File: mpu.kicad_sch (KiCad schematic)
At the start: 25 parts, among them SW401 SW_DIP_x03, U401 STM32MP135FAE7, Y401 32.768 kHz, Y402 24 MHz

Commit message: Update BOM, and fix MPU pinout
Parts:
- removed R404: 10 kΩ, Resistor_SMD:R_0201_0603Metric, symbol Device:R
- added D401, D402: 150060RS75000, LED_SMD:LED_0603_1608Metric, symbol Device:LED
- added R403: 10 kΩ, perfect_footprints:R_0201_0603Metric, symbol Device:R
- added R405, R406: 1 kΩ, perfect_footprints:R_0201_0603Metric, symbol Device:R
- added TP406, TP407: TestPoint, TestPoint:TestPoint_Pad_D1.0mm, symbol Connector:TestPoint
- C401, C402, C403, C404, C405, C406: footprint Capacitor_SMD:C_0201_0603Metric -> perfect_footprints:C_0201_0603Metric
- R401: footprint Resistor_SMD:R_0201_0603Metric -> perfect_footprints:R_0201_0603Metric
- R402: renamed from R403; footprint Resistor_SMD:R_0201_0603Metric -> perfect_footprints:R_0201_0603Metric
- R404: renamed from R402; footprint Resistor_SMD:R_0201_0603Metric -> perfect_footprints:R_0201_0603Metric; now fitted
- R407: renamed from R405; footprint Resistor_SMD:R_0201_0603Metric -> perfect_footprints:R_0201_0603Metric
- R408: renamed from R406; footprint Resistor_SMD:R_0201_0603Metric -> perfect_footprints:R_0201_0603Metric
- R409: renamed from R407; footprint Resistor_SMD:R_0201_0603Metric -> perfect_footprints:R_0201_0603Metric
- renumbered TP406 to TP408, TP407 to TP409, TP408 to TP410
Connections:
- net DEBUG.RX: now also U401.D2 (PD6), R403.2; no longer U401.B7 (PH14)
- net DEBUG.TX: now also U401.C5 (PD8); no longer U401.A2 (PA9)
- net PMIC.INT_N: now also U401.A2 (PA9); no longer U401.D2 (PD6)
- net SCREEN.DISP: now also U401.B7 (PH14); no longer U401.C5 (PD8)
- net VDD: now also D401.2 (A), D402.2 (A), R403.1
- net PA13: now reaches U401.P3 (PA13)
- net PA13: now also R405.2, TP406.1
- net PA14: now reaches U401.T12 (PA14)
- net PA14: now also R406.2, TP407.1
- new net: D402.1 (K), R406.1
- new net: D401.1 (K), R405.1
- no-connect marks 43 -> 41
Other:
- moved on the sheet: U401E

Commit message: Rework MPU power
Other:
- sheet MPU PMIC ports: added VDD_SD_IO; removed VDD_SD, V_3V3
- sheet MPU power ports: added VDD_SD_IO; removed none
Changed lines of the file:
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@@
 	)
 	(junction
+		(at 78.74 97.79)
+		(diameter 0)
+		(color 0 0 0 0)
+	)
+	(junction
 		(at 260.35 278.13)
 		(diameter 0)
@@
 	)
 	(junction
-		(at 83.82 87.63)
+		(at 83.82 85.09)
 		(diameter 0)
 		(color 0 0 0 0)
@@
 	(wire
 		(pts
+			(xy 78.74 105.41) (xy 86.36 105.41)
+		)
+		(stroke
+			(width 0)
+			(type default)
+		)
+	)
+	(wire
+		(pts
 			(xy 46.99 190.5) (xy 34.29 190.5)
 		)
@@
 		)
 	)
-	(wire
-		(pts
-			(xy 73.66 80.01) (xy 86.36 80.01)
-		)
-		(stroke
-			(width 0)
-			(type default)
-		)
-	)
 	(bus
 		(pts
@@
 	(wire
 		(pts
-			(xy 83.82 87.63) (xy 99.06 87.63)
+			(xy 83.82 85.09) (xy 99.06 85.09)
 		)
 		(stroke
@@
 	(wire
 		(pts
+			(xy 78.74 97.79) (xy 99.06 97.79)
+		)
+		(stroke
+			(width 0)
+			(type default)
+		)
+	)
+	(wire
+		(pts
 			(xy 300.99 200.66) (xy 317.5 200.66)
 		)
@@
 	(wire
 		(pts
-			(xy 86.36 85.09) (xy 83.82 85.09)
+			(xy 86.36 82.55) (xy 83.82 82.55)
 		)
 		(stroke
@@
 	(wire
 		(pts
-			(xy 83.82 85.09) (xy 83.82 87.63)
+			(xy 83.82 82.55) (xy 83.82 85.09)
 		)
 		(stroke
@@
 	(wire
 		(pts
-			(xy 73.66 82.55) (xy 86.36 82.55)
+			(xy 73.66 80.01) (xy 86.36 80.01)
 		)
 		(stroke
@@
 	(wire
 		(pts
+			(xy 78.74 97.79) (xy 78.74 105.41)
+		)
+		(stroke
+			(width 0)
+			(type default)
+		)
+	)
+	(wire
+		(pts
 			(xy 271.78 278.13) (xy 278.13 278.13)
 		)
@@
 	(wire
 		(pts
-			(xy 73.66 87.63) (xy 83.82 87.63)
+			(xy 73.66 85.09) (xy 83.82 85.09)
 		)
 		(stroke
@@
 	(wire
 		(pts
+			(xy 73.66 97.79) (xy 78.74 97.79)
+		)
+		(stroke
+			(width 0)
+			(type default)
+		)
+	)
+	(wire
+		(pts
 			(xy 87.63 165.1) (xy 100.33 165.1)
 		)
@@
 	(wire
 		(pts
-			(xy 25.4 69.85) (xy 25.4 74.93)
-		)
-		(stroke
-			(width 0)
-			(type default)
-		)
-	)
-	(wire
-		(pts
 			(xy 300.99 144.78) (xy 317.5 144.78)
 		)
@@
 	(wire
 		(pts
-			(xy 73.66 97.79) (xy 99.06 97.79)
+			(xy 73.66 87.63) (xy 99.06 87.63)
 		)
 		(stroke
@@
 		)
 	)
-	(wire
-		(pts
-			(xy 25.4 74.93) (xy 35.56 74.93)
-		)
-		(stroke
-			(width 0)
-			(type default)
-		)
-	)
 	(bus
 		(pts
@@
 		)
 	)
+	(hierarchical_label "VDD_SD_IO"
+		(shape output)
+		(at 86.36 105.41 0)
+		(effects
+			(font
+				(size 1.27 1.27)
+			)
+			(justify left)
+		)
+	)
 	(hierarchical_label "{DDR}"
 		(shape bidirectional)
@@
 		)
 	)
-	(hierarchical_label "VDD_SD"
-		(shape output)
-		(at 86.36 80.01 0)
-		(effects
-			(font
-				(size 1.27 1.27)
-			)
-			(justify left)
-		)
-	)
 	(hierarchical_label "{WLAN}"
 		(shape bidirectional)
@@
 	(hierarchical_label "VDD"
 		(shape output)
-		(at 86.36 85.09 0)
+		(at 86.36 82.55 0)
 		(effects
 			(font
@@
 	(hierarchical_label "VREF_DDR"
 		(shape output)
-		(at 86.36 82.55 0)
+		(at 86.36 80.01 0)
 		(effects
 			(font
@@
 		(on_board yes)
 		(dnp no)
-		(property "Reference" "#PWR0402"
+		(property "Reference" "#PWR0401"
 			(at 31.75 73.66 0)
 			(effects
@@
 			(project "linux-sbc"
 				(path "/fa11a02f-8043-4153-ab69-88d766503017/2d01087b-54dc-4f43-9cc7-a0ba17201776"
-					(reference "#PWR0402")
+					(reference "#PWR0401")
 					(unit 1)
 				)
@@
 	)
 	(symbol
-		(lib_id "power:VCC")
-		(at 25.4 69.85 0)
-		(unit 1)
-		(exclude_from_sim no)
-		(in_bom yes)
-		(on_board yes)
-		(dnp no)
-		(property "Reference" "#PWR0401"
-			(at 25.4 73.66 0)
-			(effects
-				(font
-					(size 1.27 1.27)
-				)
-				(hide yes)
-			)
-		)
-		(property "Value" "V_3V3"
-			(at 25.4 66.802 0)
-			(effects
-				(font
-					(size 1.27 1.27)
-				)
-				(justify bottom)
-			)
-		)
-		(property "Footprint" ""
-			(at 25.4 69.85 0)
-			(effects
-				(font
-					(size 1.27 1.27)
-				)
-				(hide yes)
-			)
-		)
-		(property "Datasheet" ""
-			(at 25.4 69.85 0)
-			(effects
-				(font
-					(size 1.27 1.27)
-				)
-				(hide yes)
-			)
-		)
-		(property "Description" "Power symbol creates a global label with name \"VCC\""
-			(at 25.4 69.85 0)
-			(effects
-				(font
-					(size 1.27 1.27)
-				)
-				(hide yes)
-			)
-		)
-		(pin "1"
-		)
-		(instances
-			(project "linux-sbc"
-				(path "/fa11a02f-8043-4153-ab69-88d766503017/2d01087b-54dc-4f43-9cc7-a0ba17201776"
-					(reference "#PWR0401")
-					(unit 1)
-				)
-			)
-		)
-	)
-	(symbol
 		(lib_name "R_1")
 		(lib_id "Device:R")
@@
 		(dnp no)
 		(fields_autoplaced yes)
-		(property "Reference" "#PWR0408"
+		(property "Reference" "#PWR0407"
 			(at 284.48 285.75 0)
 			(effects
@@
 			(project "linux-sbc"
 				(path "/fa11a02f-8043-4153-ab69-88d766503017/2d01087b-54dc-4f43-9cc7-a0ba17201776"
-					(reference "#PWR0408")
+					(reference "#PWR0407")
 					(unit 1)
 				)
@@
 		(dnp no)
 		(fields_autoplaced yes)
-		(property "Reference" "#PWR0409"
+		(property "Reference" "#PWR0408"
 			(at 401.32 114.3 0)
 			(effects
@@
 			(project "linux-sbc"
 				(path "/fa11a02f-8043-4153-ab69-88d766503017/2d01087b-54dc-4f43-9cc7-a0ba17201776"
-					(reference "#PWR0409")
+					(reference "#PWR0408")
 					(unit 1)
 				)
@@
 		(dnp no)
 		(fields_autoplaced yes)
-		(property "Reference" "#PWR0407"
+		(property "Reference" "#PWR0406"
 			(at 209.55 101.6 0)
 			(effects
@@
 			(project "linux-sbc"
 				(path "/fa11a02f-8043-4153-ab69-88d766503017/2d01087b-54dc-4f43-9cc7-a0ba17201776"
-					(reference "#PWR0407")
+					(reference "#PWR0406")
 					(unit 1)
 				)
@@
 		(dnp no)
 		(fields_autoplaced yes)
-		(property "Reference" "#PWR0403"
+		(property "Reference" "#PWR0402"
 			(at 97.79 247.65 0)
 			(effects
@@
 			(project "linux-sbc"
 				(path "/fa11a02f-8043-4153-ab69-88d766503017/2d01087b-54dc-4f43-9cc7-a0ba17201776"
-					(reference "#PWR0403")
+					(reference "#PWR0402")
 					(unit 1)
 				)
@@
 		(dnp no)
 		(fields_autoplaced yes)
-		(property "Reference" "#PWR0405"
+		(property "Reference" "#PWR0404"
 			(at 144.78 110.49 0)
 			(effects
@@
 			(project "linux-sbc"
 				(path "/fa11a02f-8043-4153-ab69-88d766503017/2d01087b-54dc-4f43-9cc7-a0ba17201776"
-					(reference "#PWR0405")
+					(reference "#PWR0404")
 					(unit 1)
 				)
@@
 		(dnp no)
 		(fields_autoplaced yes)
-		(property "Reference" "#PWR0404"
+		(property "Reference" "#PWR0403"
 			(at 102.87 245.11 0)
 			(effects
@@
 			(project "linux-sbc"
 				(path "/fa11a02f-8043-4153-ab69-88d766503017/2d01087b-54dc-4f43-9cc7-a0ba17201776"
-					(reference "#PWR0404")
+					(reference "#PWR0403")
 					(unit 1)
 				)
@@
 		(dnp no)
 		(fields_autoplaced yes)
-		(property "Reference" "#PWR0406"
+		(property "Reference" "#PWR0405"
 			(at 157.48 110.49 0)
 			(effects
@@
 			(project "linux-sbc"
 				(path "/fa11a02f-8043-4153-ab69-88d766503017/2d01087b-54dc-4f43-9cc7-a0ba17201776"
-					(reference "#PWR0406")
+					(reference "#PWR0405")
 					(unit 1)
 				)
@@
 	)
 	(sheet
-		(at 99.06 85.09)
-		(size 25.4 17.78)
+		(at 99.06 82.55)
+		(size 25.4 20.32)
 		(exclude_from_sim no)
 		(in_bom yes)
@@
 		)
 		(property "Sheetname" "MPU power"
-			(at 99.06 84.2046 0)
+			(at 99.06 81.6646 0)
 			(effects
 				(font
@@
 		)
 		(pin "VDD" input
-			(at 99.06 87.63 180)
+			(at 99.06 85.09 180)
 			(effects
 				(font
@@
 		)
 		(pin "VDD_USB" input
+			(at 99.06 87.63 180)
+			(effects
+				(font
+					(size 1.27 1.27)
+				)
+				(justify left)
+			)
+		)
+		(pin "VDD_SD_IO" input
 			(at 99.06 97.79 180)
 			(effects
@@
 			)
 		)
-		(pin "V_3V3" input
-			(at 35.56 74.93 180)
-			(effects
-				(font
-					(size 1.27 1.27)
-				)
-				(justify left)
-			)
-		)
 		(pin "V_5V0" input
 			(at 35.56 72.39 180)
@@
 		)
 		(pin "VDD" output
-			(at 73.66 87.63 0)
+			(at 73.66 85.09 0)
 			(effects
 				(font
@@
 			)
 		)
-		(pin "VDD_SD" output
-			(at 73.66 80.01 0)
+		(pin "VDD_USB" output
+			(at 73.66 87.63 0)
 			(effects
 				(font
@@
 			)
 		)
-		(pin "VDD_USB" output
-			(at 73.66 97.79 0)
+		(pin "VREF_DDR" output
+			(at 73.66 80.01 0)
 			(effects
 				(font
@@
 			)
 		)
-		(pin "VREF_DDR" output
-			(at 73.66 82.55 0)
+		(pin "VDD_SD_IO" output
+			(at 73.66 97.79 0)
 			(effects
 				(font

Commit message: Rework the schematics
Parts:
- renumbered C401 to C501, C402 to C502, C403 to C503, C404 to C504, C405 to C505, C406 to C506, D401 to D501, D402 to D502, R401 to R501, R402 to R502, R403 to R503, R404 to R504, R405 to R505, R406 to R506, R407 to R507, R408 to R508, R409 to R509, SW401 to SW501, TP401 to TP501, TP402 to TP502, TP403 to TP503, TP404 to TP504, TP405 to TP505, TP406 to TP506, TP407 to TP507, TP408 to TP508, TP409 to TP509, TP410 to TP510, U401 to U501, Y401 to Y501, Y402 to Y502
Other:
- removed sheet MPU PMIC

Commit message: Rework text boxes
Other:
- note added: "Boot selection"
- note added: "Clocks"
- note added: "DDR"
- note added: "IO"
- note added: "Miscellaneous"
- note added: "Notes"
- note added: "Power"
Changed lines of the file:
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@@
 		(members "USB.DP" "USB.DN")
 	)
-	(text_box "Clocks"
-		(exclude_from_sim no)
-		(at 152.4 251.46 0)
-		(size 146.05 33.02)
-		(margins 0.9525 2 0.9525 0.9525)
-		(stroke
-			(width 0)
-			(type solid)
-		)
-		(fill
-			(type none)
-		)
-		(effects
-			(font
-				(size 5.08 5.08)
-				(thickness 1.016)
-				(bold yes)
-			)
-			(justify left top)
-		)
-	)
-	(text_box "Notes"
-		(exclude_from_sim no)
-		(at 12.7 251.46 0)
-		(size 139.7 33.02)
-		(margins 0.9525 2 0.9525 0.9525)
-		(stroke
-			(width 0)
-			(type solid)
-		)
-		(fill
-			(type none)
-		)
-		(effects
-			(font
-				(size 5.08 5.08)
-				(thickness 1.016)
-				(bold yes)
-			)
-			(justify top)
-		)
-	)
-	(text_box "Power"
-		(exclude_from_sim no)
-		(at 12.7 50.8 0)
-		(size 114.3 63.5)
-		(margins 0.9525 2 0.9525 0.9525)
-		(stroke
-			(width 0)
-			(type solid)
-		)
-		(fill
-			(type none)
-		)
-		(effects
-			(font
-				(size 5.08 5.08)
-				(thickness 1.016)
-				(bold yes)
-			)
-			(justify top)
+	(rectangle
+		(start 12.7 251.46)
+		(end 152.4 284.48)
+		(stroke
+			(width 0)
+			(type default)
+		)
+		(fill
+			(type none)
+		)
+	)
+	(rectangle
+		(start 12.7 50.8)
+		(end 127 114.3)
+		(stroke
+			(width 0)
+			(type default)
+		)
+		(fill
+			(type none)
+		)
+	)
+	(rectangle
+		(start 12.7 114.3)
+		(end 127 251.46)
+		(stroke
+			(width 0)
+			(type default)
+		)
+		(fill
+			(type none)
+		)
+	)
+	(rectangle
+		(start 241.3 50.8)
+		(end 406.4 114.3)
+		(stroke
+			(width 0)
+			(type default)
+		)
+		(fill
+			(type none)
+		)
+	)
+	(rectangle
+		(start 127 114.3)
+		(end 406.4 251.46)
+		(stroke
+			(width 0)
+			(type default)
+		)
+		(fill
+			(type none)
+		)
+	)
+	(rectangle
+		(start 152.4 251.46)
+		(end 298.45 284.48)
+		(stroke
+			(width 0)
+			(type default)
+		)
+		(fill
+			(type none)
+		)
+	)
+	(rectangle
+		(start 127 50.8)
+		(end 241.3 114.3)
+		(stroke
+			(width 0)
+			(type default)
+		)
+		(fill
+			(type none)
+		)
+	)
+	(text "Miscellaneous"
+		(exclude_from_sim no)
+		(at 128.27 53.34 0)
+		(effects
+			(font
+				(size 5.08 5.08)
+				(thickness 1.016)
+				(bold yes)
+			)
+			(justify left top)
+		)
+	)
+	(text "Notes"
+		(exclude_from_sim no)
+		(at 13.97 254 0)
+		(effects
+			(font
+				(size 5.08 5.08)
+				(thickness 1.016)
+				(bold yes)
+			)
+			(justify left top)
+		)
+	)
+	(text "Clocks"
+		(exclude_from_sim no)
+		(at 153.67 254 0)
+		(effects
+			(font
+				(size 5.08 5.08)
+				(thickness 1.016)
+				(bold yes)
+			)
+			(justify left top)
+		)
+	)
+	(text "Boot selection"
+		(exclude_from_sim no)
+		(at 242.57 53.34 0)
+		(effects
+			(font
+				(size 5.08 5.08)
+				(thickness 1.016)
+				(bold yes)
+			)
+			(justify left top)
+		)
+	)
+	(text "IO"
+		(exclude_from_sim no)
+		(at 128.27 116.84 0)
+		(effects
+			(font
+				(size 5.08 5.08)
+				(thickness 1.016)
+				(bold yes)
+			)
+			(justify left top)
+		)
+	)
+	(text "Power"
+		(exclude_from_sim no)
+		(at 13.97 53.34 0)
+		(effects
+			(font
+				(size 5.08 5.08)
+				(thickness 1.016)
+				(bold yes)
+			)
+			(justify left top)
+		)
+	)
+	(text "DDR"
+		(exclude_from_sim no)
+		(at 13.97 116.84 0)
+		(effects
+			(font
+				(size 5.08 5.08)
+				(thickness 1.016)
+				(bold yes)
+			)
+			(justify left top)
 		)
 	)
@@
 		)
 	)
-	(text_box "Boot selection"
-		(exclude_from_sim no)
-		(at 241.3 50.8 0)
-		(size 165.1 63.5)
-		(margins 0.9525 2 0.9525 0.9525)
-		(stroke
-			(width 0)
-			(type solid)
-		)
-		(fill
-			(type none)
-		)
-		(effects
-			(font
-				(size 5.08 5.08)
-				(thickness 1.016)
-				(bold yes)
-			)
-			(justify top)
-		)
-	)
-	(text_box "DDR"
-		(exclude_from_sim no)
-		(at 12.7 114.3 0)
-		(size 114.3 137.16)
-		(margins 0.9525 2 0.9525 0.9525)
-		(stroke
-			(width 0)
-			(type solid)
-		)
-		(fill
-			(type none)
-		)
-		(effects
-			(font
-				(size 5.08 5.08)
-				(thickness 1.016)
-				(bold yes)
-			)
-			(justify top)
-		)
-	)
-	(text_box "IO"
-		(exclude_from_sim no)
-		(at 127 114.3 0)
-		(size 279.4 137.16)
-		(margins 0.9525 2 0.9525 0.9525)
-		(stroke
-			(width 0)
-			(type solid)
-		)
-		(fill
-			(type none)
-		)
-		(effects
-			(font
-				(size 5.08 5.08)
-				(thickness 1.016)
-				(bold yes)
-			)
-			(justify top)
-		)
-	)
-	(text_box "Miscellaneous"
-		(exclude_from_sim no)
-		(at 127 50.8 0)
-		(size 114.3 63.5)
-		(margins 0.9525 2 0.9525 0.9525)
-		(stroke
-			(width 0)
-			(type solid)
-		)
-		(fill
-			(type none)
-		)
-		(effects
-			(font
-				(size 5.08 5.08)
-				(thickness 1.016)
-				(bold yes)
-			)
-			(justify top)
-		)
-	)

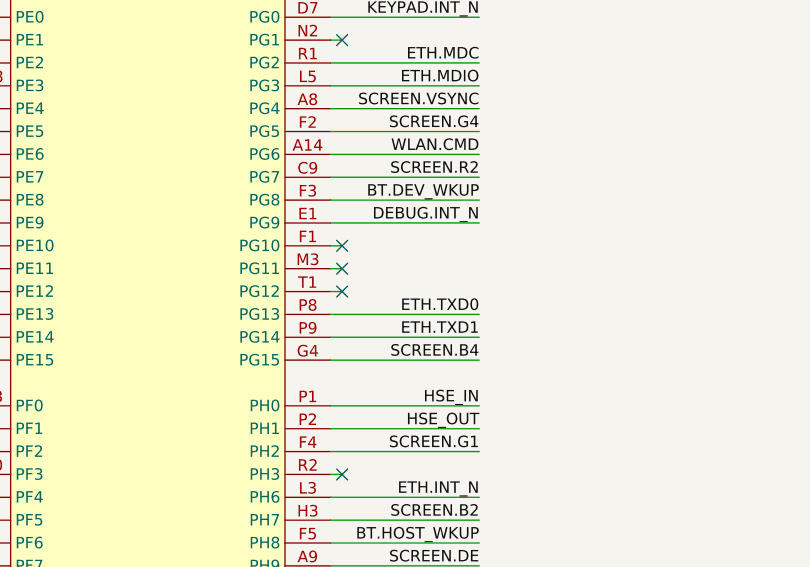
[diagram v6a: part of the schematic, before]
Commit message: Fix ethernet
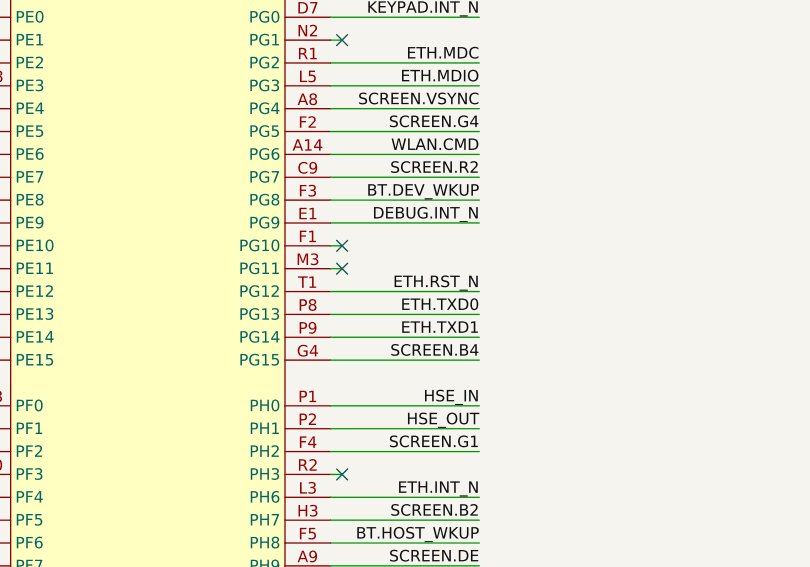
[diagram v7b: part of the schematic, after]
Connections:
- net ETH.RST_N: now also U501.T1 (PG12)
- no-connect marks 41 -> 40
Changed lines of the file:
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@@
 	)
 	(no_connect
-		(at 302.26 157.48)
-	)
-	(no_connect
 		(at 166.37 86.36)
 	)
@@
 	(wire
 		(pts
-			(xy 300.99 157.48) (xy 302.26 157.48)
+			(xy 300.99 157.48) (xy 317.5 157.48)
 		)
 		(stroke
@@
 		)
 	)
+	(label "ETH.RST_N"
+		(at 317.5 157.48 180)
+		(effects
+			(font
+				(size 1.27 1.27)
+			)
+			(justify right bottom)
+		)
+	)

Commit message: Fix PMIC.WKUP
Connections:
- net PMIC.WKUP: now also U501.K4 (PC13); no longer U501.E3 (PA12)
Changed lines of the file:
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@@
 	)
 	(no_connect
+		(at 156.21 157.48)
+	)
+	(no_connect
 		(at 302.26 129.54)
 	)
@@
 	)
 	(no_connect
-		(at 199.39 160.02)
-	)
-	(no_connect
 		(at 302.26 223.52)
 	)
@@
 		)
 	)
-	(wire
+	(bus
 		(pts
-			(xy 142.24 157.48) (xy 157.48 157.48)
+			(xy 170.18 243.84) (xy 170.18 246.38)
 		)
 		(stroke
@@
 		)
 	)
-	(bus
+	(wire
 		(pts
-			(xy 170.18 243.84) (xy 170.18 246.38)
+			(xy 198.12 154.94) (xy 215.9 154.94)
 		)
 		(stroke
@@
 	(wire
 		(pts
-			(xy 198.12 154.94) (xy 215.9 154.94)
+			(xy 156.21 157.48) (xy 157.48 157.48)
 		)
 		(stroke
@@
 	(wire
 		(pts
-			(xy 198.12 160.02) (xy 199.39 160.02)
+			(xy 198.12 160.02) (xy 215.9 160.02)
 		)
 		(stroke
@@
 	)
 	(label "PMIC.WKUP"
-		(at 142.24 157.48 0)
+		(at 215.9 160.02 180)
 		(effects
 			(font
 				(size 1.27 1.27)
 			)
-			(justify left bottom)
+			(justify right bottom)
 		)
 	)
